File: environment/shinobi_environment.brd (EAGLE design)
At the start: 40.5 x 35 mm, 11 parts

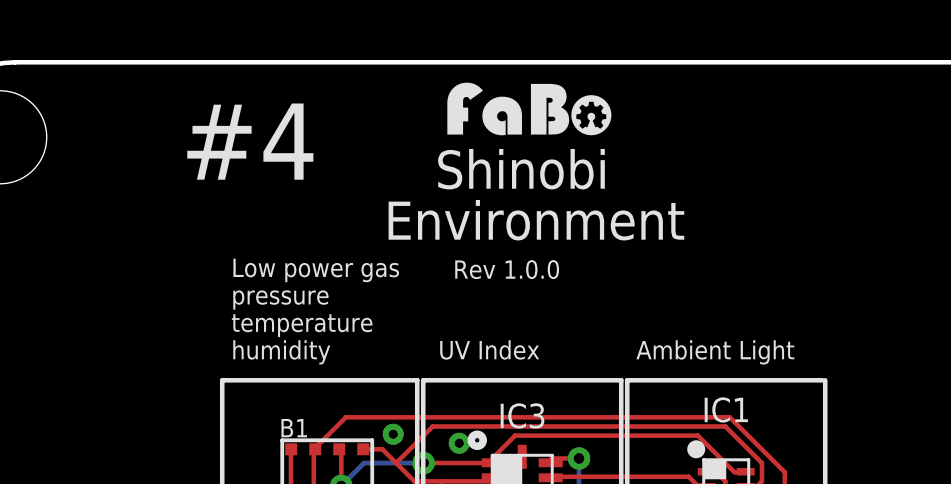
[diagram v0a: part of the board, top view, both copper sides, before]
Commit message: Update BLE with connector.
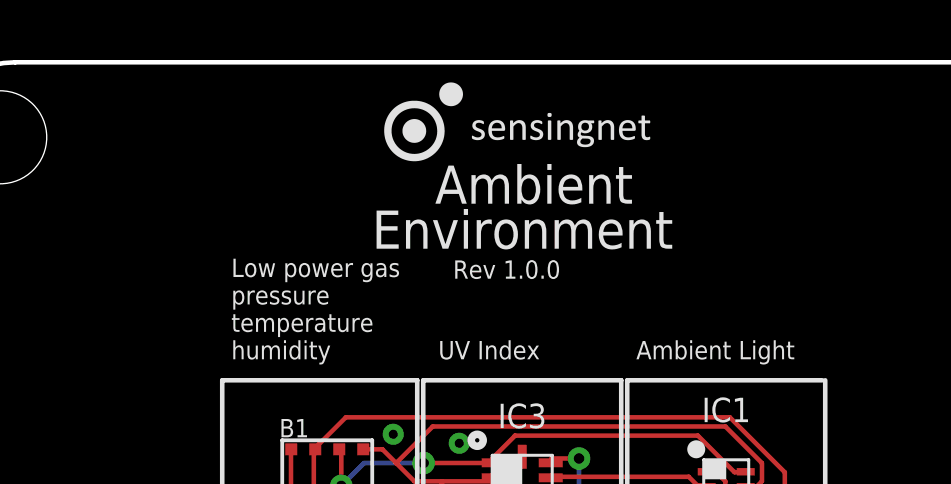
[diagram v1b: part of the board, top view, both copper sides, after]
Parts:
- U$2: device FaBo-Logo:LOGO_FABO_S -> sensingnet:LOGO_WHITE
- moved U$2 4.95 mm to (15.3, 31.7)
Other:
- board text added: "Ambient"
- board text removed: "#4"
- board text removed: "Shinobi"
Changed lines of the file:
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@@
 <?xml version="1.0" encoding="utf-8"?>
 <!DOCTYPE eagle SYSTEM "eagle.dtd">
-<eagle version="8.2.2">
+<eagle version="9.0.0">
 <drawing>
 <settings>
-<setting alwaysvectorfont="no"/>
+<setting alwaysvectorfont="yes"/>
+<setting keepoldvectorfont="yes"/>
 <setting verticaltext="up"/>
 </settings>
@@
 <layers>
 <layer number="1" name="Top" color="4" fill="1" visible="yes" active="yes"/>
+<layer number="2" name="Route2" color="1" fill="3" visible="no" active="yes"/>
+<layer number="15" name="Route15" color="4" fill="6" visible="no" active="yes"/>
 <layer number="16" name="Bottom" color="1" fill="1" visible="yes" active="yes"/>
 <layer number="17" name="Pads" color="2" fill="1" visible="yes" active="yes"/>
@@
 <layer number="59" name="tCarbon" color="7" fill="1" visible="no" active="no"/>
 <layer number="60" name="bCarbon" color="7" fill="1" visible="no" active="no"/>
+<layer number="88" name="SimResults" color="9" fill="1" visible="no" active="no"/>
+<layer number="89" name="SimProbes" color="9" fill="1" visible="no" active="no"/>
 <layer number="90" name="Modules" color="5" fill="1" visible="no" active="no"/>
 <layer number="91" name="Nets" color="2" fill="1" visible="no" active="no"/>
@@
 <board>
 <plain>
-<text x="16.992" y="30.786" size="1.27" layer="21">Shinobi</text>
-<text x="15.292" y="29.086" size="1.27" layer="21">Environment</text>
+<text x="16.992" y="30.286" size="1.27" layer="21">Ambient</text>
+<text x="14.892" y="28.786" size="1.27" layer="21">Environment</text>
 <wire x1="9.9" y1="24.4" x2="16.4" y2="24.4" width="0.1524" layer="21"/>
 <wire x1="16.4" y1="24.4" x2="16.4" y2="14.7" width="0.1524" layer="21"/>
@@
 <wire x1="30" y1="24.4" x2="30" y2="14.7" width="0.1524" layer="21"/>
 <text x="23.7" y="25.1" size="0.6096" layer="21">Ambient Light</text>
-<text x="8.492" y="31.086" size="2.54" layer="21">#4</text>
 <text x="17.592" y="27.786" size="0.6096" layer="21">Rev 1.0.0</text>
 </plain>
@@
 <param name="dpMaxLengthDifference" value="10mm"/>
 <param name="dpGapFactor" value="2.5"/>
-<param name="checkGrid" value="0"/>
 <param name="checkAngle" value="0"/>
 <param name="checkFont" value="1"/>
 <param name="checkRestrict" value="1"/>
+<param name="checkStop" value="0"/>
+<param name="checkValues" value="0"/>
 <param name="useDiameter" value="13"/>
 <param name="maxErrors" value="50"/>
@@
 </autorouter>
 <elements>
-<element name="U$2" library="FaBo-Logo" package="LOGO_FABO_S" value="" x="20.2" y="32.418"/>
 <element name="I2C" library="FaBo-Template" package="FABO_BRICK_I2C_S04B-PASK-2_LONG" value="" x="20.25" y="6.7" rot="R180"/>
 <element name="B1" library="FaBo-Mems" package="BOSCH-BME680" value="" x="13.4" y="20.9"/>
@@
 <element name="C2" library="FaBo-Capacitor" package="0603" value="1uF" x="25.5" y="17"/>
 <element name="U$3" library="FaBo-Template" package="FABO-SHINOBI" value="" x="0" y="0"/>
+<element name="U$2" library="sensingnet" package="LOGO_WHITE" value="" x="15.3" y="31.7"/>
 </elements>
 <signals>

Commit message: シルク削除
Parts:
- removed U$2: (no value), sensingnet:LOGO_WHITE
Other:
- board text removed: "Ambient"
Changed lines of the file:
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@@
 <?xml version="1.0" encoding="utf-8"?>
 <!DOCTYPE eagle SYSTEM "eagle.dtd">
-<eagle version="9.0.0">
+<eagle version="9.6.0">
 <drawing>
 <settings>
-<setting alwaysvectorfont="yes"/>
+<setting alwaysvectorfont="no"/>
 <setting keepoldvectorfont="yes"/>
 <setting verticaltext="up"/>
@@
 <board>
 <plain>
-<text x="16.992" y="30.286" size="1.27" layer="21">Ambient</text>
 <text x="14.892" y="28.786" size="1.27" layer="21">Environment</text>
 <wire x1="9.9" y1="24.4" x2="16.4" y2="24.4" width="0.1524" layer="21"/>
@@
 <param name="checkStop" value="0"/>
 <param name="checkValues" value="0"/>
+<param name="checkNames" value="1"/>
+<param name="checkWireStubs" value="1"/>
+<param name="checkPolygonWidth" value="0"/>
 <param name="useDiameter" value="13"/>
 <param name="maxErrors" value="50"/>
@@
 </autorouter>
 <elements>
-<element name="I2C" library="FaBo-Template" package="FABO_BRICK_I2C_S04B-PASK-2_LONG" value="" x="20.25" y="6.7" rot="R180"/>
-<element name="B1" library="FaBo-Mems" package="BOSCH-BME680" value="" x="13.4" y="20.9"/>
-<element name="C1" library="FaBo-Capacitor" package="0603" value="100nf" x="13.4" y="17.1"/>
-<element name="IC3" library="FaBo-Mems" package="SILICONLABS-SI1133" value="" x="19.9" y="20.9"/>
-<element name="C3" library="FaBo-Capacitor" package="0603" value="0.1uF" x="19" y="17.2" rot="R180"/>
-<element name="R4" library="FaBo-Resistors" package="0603" value="10k" x="21.9" y="18" rot="R90"/>
-<element name="IC1" library="FaBo-Mems" package="INTERSIL-ISL29034" value="" x="26.7" y="21.1"/>
-<element name="R1" library="FaBo-Resistors" package="0603" value="100" x="28.7" y="17.8" rot="R90"/>
-<element name="C2" library="FaBo-Capacitor" package="0603" value="1uF" x="25.5" y="17"/>
-<element name="U$3" library="FaBo-Template" package="FABO-SHINOBI" value="" x="0" y="0"/>
-<element name="U$2" library="sensingnet" package="LOGO_WHITE" value="" x="15.3" y="31.7"/>
+<element name="I2C" library="FaBo-Template" package="FABO_BRICK_I2C_S04B-PASK-2_LONG" value="" x="20.25" y="6.7" smashed="yes" rot="R180">
+<attribute name="NAME" x="20.25" y="10.51" size="0.8128" layer="25" font="vector" ratio="12" align="bottom-center"/>
+</element>
+<element name="B1" library="FaBo-Mems" package="BOSCH-BME680" value="" x="13.4" y="20.9" smashed="yes">
+<attribute name="NAME" x="11.8" y="22.5" size="0.6096" layer="25"/>
+</element>
+<element name="C1" library="FaBo-Capacitor" package="0603" value="100nf" x="13.4" y="17.1" smashed="yes">
+<attribute name="NAME" x="13.4" y="17.989" size="0.8128" layer="25" font="vector" ratio="12" align="bottom-center"/>
+<attribute name="VALUE" x="13.4" y="17.1" size="0.8128" layer="27" font="vector" ratio="12" align="center"/>
+</element>
+<element name="IC3" library="FaBo-Mems" package="SILICONLABS-SI1133" value="" x="19.9" y="20.9" smashed="yes">
+<attribute name="NAME" x="19.9" y="22.805" size="0.8128" layer="21" font="vector" ratio="12" align="bottom-center"/>
+</element>
+<element name="C3" library="FaBo-Capacitor" package="0603" value="0.1uF" x="19" y="17.2" smashed="yes" rot="R180">
+<attribute name="NAME" x="19" y="16.311" size="0.8128" layer="25" font="vector" ratio="12" rot="R180" align="bottom-center"/>
+<attribute name="VALUE" x="19" y="17.2" size="0.8128" layer="27" font="vector" ratio="12" rot="R180" align="center"/>
+</element>
+<element name="R4" library="FaBo-Resistors" package="0603" value="10k" x="21.9" y="18" smashed="yes" rot="R90">
+<attribute name="NAME" x="21.011" y="18" size="0.8128" layer="25" font="vector" ratio="12" rot="R90" align="bottom-center"/>
+<attribute name="VALUE" x="21.9" y="18" size="0.8128" layer="27" font="vector" ratio="12" rot="R90" align="center"/>
+</element>
+<element name="IC1" library="FaBo-Mems" package="INTERSIL-ISL29034" value="" x="26.7" y="21.1" smashed="yes">
+<attribute name="NAME" x="26.7" y="23.005" size="0.8128" layer="25" font="vector" ratio="12" rot="SR0" align="bottom-center"/>
+</element>
+<element name="R1" library="FaBo-Resistors" package="0603" value="100" x="28.7" y="17.8" smashed="yes" rot="R90">
+<attribute name="NAME" x="27.811" y="17.8" size="0.8128" layer="25" font="vector" ratio="12" rot="R90" align="bottom-center"/>
+<attribute name="VALUE" x="28.7" y="17.8" size="0.8128" layer="27" font="vector" ratio="12" rot="R90" align="center"/>
+</element>
+<element name="C2" library="FaBo-Capacitor" package="0603" value="1uF" x="25.5" y="17" smashed="yes">
+<attribute name="NAME" x="25.5" y="17.889" size="0.8128" layer="25" font="vector" ratio="12" align="bottom-center"/>
+<attribute name="VALUE" x="25.5" y="17" size="0.8128" layer="27" font="vector" ratio="12" align="center"/>
+</element>
+<element name="U$3" library="FaBo-Template" package="FABO-SHINOBI" value="" x="0" y="0" smashed="yes"/>
 </elements>
 <signals>
@@
 </signal>
 </signals>
+<mfgpreviewcolors>
+<mfgpreviewcolor name="soldermaskcolor" color="0xC8008000"/>
+<mfgpreviewcolor name="silkscreencolor" color="0xFFFEFEFE"/>
+<mfgpreviewcolor name="backgroundcolor" color="0xFF282828"/>
+<mfgpreviewcolor name="coppercolor" color="0xFFFFBF00"/>
+<mfgpreviewcolor name="substratecolor" color="0xFF786E46"/>
+</mfgpreviewcolors>
 </board>
 </drawing>

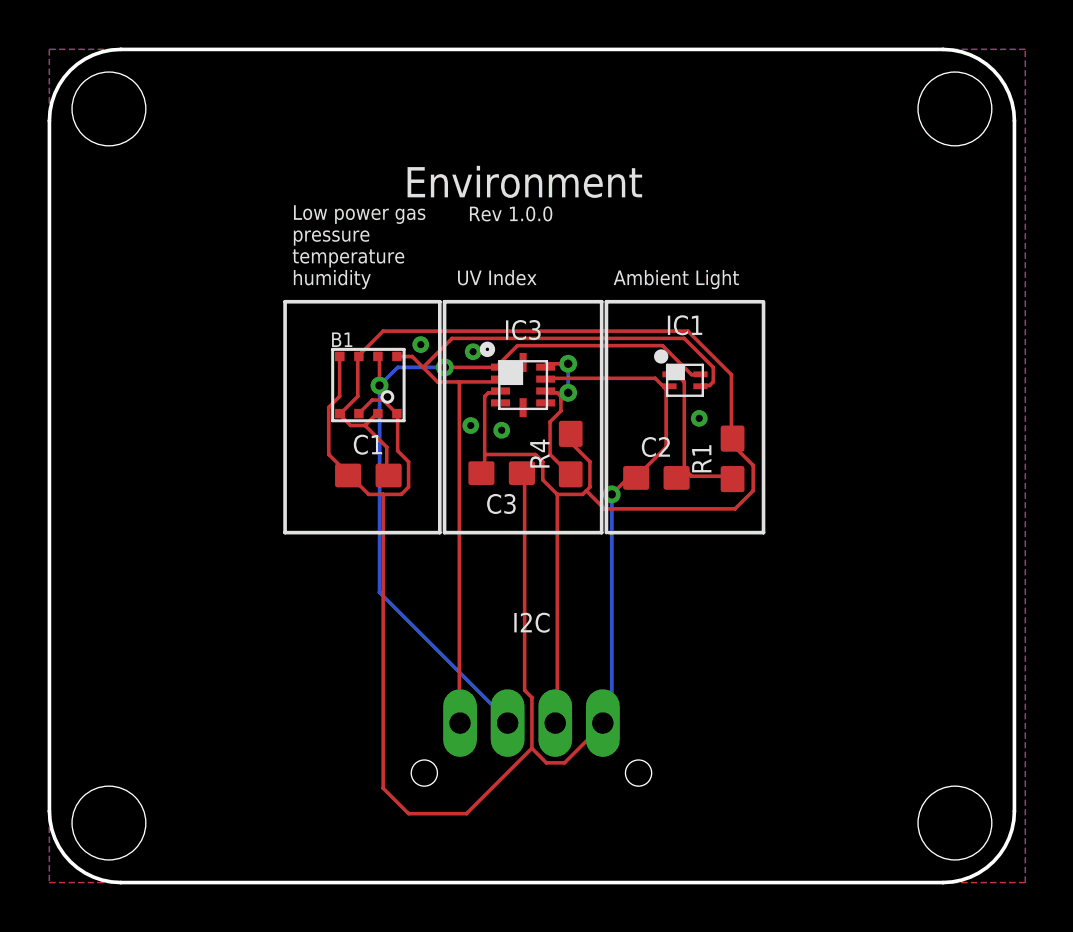
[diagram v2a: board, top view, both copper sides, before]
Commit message: #21 Shinobi Enviroment 1.0.1 アップデート　VCC ５V対応　LDO、レベル変換、BME６８０通風口追加、番号の変更　４から２１
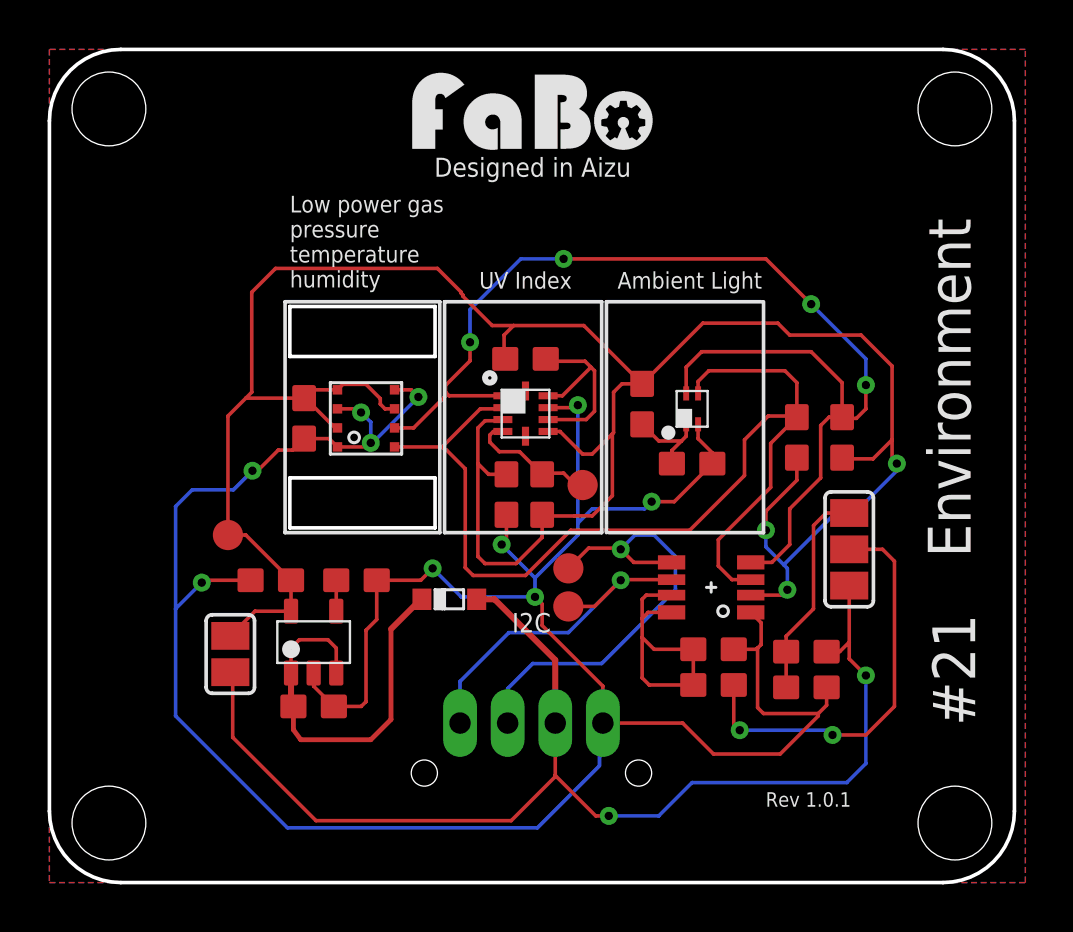
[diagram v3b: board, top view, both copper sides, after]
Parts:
- added C4: 0.01uF, FaBo-Capacitor:0603
- added C5: 1uF, FaBo-Capacitor:0603
- added C6: 4.7uF, FaBo-Capacitor:0603
- added C7: 0.1uF, FaBo-Capacitor:0603
- added IC2: (no value), FaBo-Supply:SOT-23-5
- added R2: 10k, FaBo-Resistors:0603
- added R3: 200k, FaBo-Resistors:0603
- added R5, R6: 4.7k, FaBo-Resistors:0603
- added R7: 1.8k, FaBo-Resistors:0603
- added R8: 3.3k, FaBo-Resistors:0603
- added SJ1: (no value), jumper:SJ_2
- added SJ2: (no value), jumper:SJ
- added TP1, TP2, TP3, TP4: TPB1,27, testpad:B1,27
- added U$14: (no value), FaBo-etc:LOGO_FABO_MS
- added U$2: CUS05F40, FaBo-Diode:CUS05F40
- added U4: PCA9306DP1, FaBo-LevelTranslator:TSSOP8
- moved R1 4.44 mm to (24.9, 20.1)
- moved R4 4.43 mm to (20.0, 22.0), turned to 180 degrees
- moved C1 3.61 mm to (10.7, 19.5), turned to 90 degrees
- moved C2 1.62 mm to (27.0, 17.6), turned to 180 degrees
- moved B1 1.40 mm to (13.3, 19.5), turned to 270 degrees
- moved IC1 1.24 mm to (27.0, 19.9), turned to 90 degrees
- moved IC3 1.20 mm to (20.0, 19.7)
- moved C3 0.92 mm to (19.2, 16.3), turned to 90 degrees
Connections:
- new net 3.3V: R7.1, R8.2, SJ1.3
- new net 5V: I2C.VCC, R7.2, SJ1.1, SJ2.1, U$2.A
- new net N$2: C4.2, IC2.4
- new net N$3: C5.2, IC2.1, IC2.3, U$2.C
- new net N$5: IC3.4, R2.1, TP4.TP
- new net N$8: C7.2, R3.1, U4.EN, U4.VREF2
- new net N$9: R3.2, SJ1.2
- new net SCL_HV: I2C.SCL, TP1.TP, U4.SCL2
- new net SDA_HV: I2C.SDA, TP2.TP, U4.SDA2
- net +3V3: now also C6.2, IC2.5, IC3.6, R2.2, R5.2, R6.2, SJ2.2, TP3.TP, U4.VREF1; no longer I2C.VCC
- net GND: now also C4.1, C5.1, C6.1, C7.1, IC2.2, R8.1, U4.GND
- net SCL: now also R5.1, U4.SCL1; no longer I2C.SCL
- net SDA: now also R6.1, U4.SDA1; no longer I2C.SDA
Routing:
- net 5V: track 0.00 -> 51.3 mm, vias 0 -> 2
- net +3V3: track 59.2 -> 106.2 mm, vias 0 -> 3
- net GND: track 70.5 -> 115.0 mm, vias 6 -> 10
- net SDA_HV: track 0.00 -> 19.5 mm, vias 0 -> 1
- net SDA: track 32.7 -> 50.2 mm, vias 2 -> 4
- net N$9: track 0.00 -> 17.3 mm, vias 0 -> 2
- net N$3: track 0.00 -> 17.2 mm
- net SCL_HV: track 0.00 -> 15.1 mm, vias 0 -> 1
- net N$8: track 0.00 -> 12.1 mm
- net SCL: track 33.6 -> 44.2 mm
- net 3.3V: track 0.00 -> 8.99 mm
- net N$5: track 0.00 -> 5.60 mm
- net VCC: track 7.56 -> 3.91 mm
- net N$2: track 0.00 -> 1.30 mm
- net N$4: track 7.30 -> 8.35 mm, vias 2 -> 0
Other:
- board text added: "#21"
- board text added: "Designed in Aizu"
- board text added: "Rev 1.0.1"
- board text removed: "Rev 1.0.0"

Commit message: ファイル削除
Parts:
- removed R4: 10k, FaBo-Resistors:0603
- removed R7: 1.8k, FaBo-Resistors:0603
- removed R8: 3.3k, FaBo-Resistors:0603
- added C8: 100nf, FaBo-Capacitor:0603
- moved U$2 10.0 mm to (12.6, 2.80)
- moved IC2 3.20 mm to (11.2, 6.90)
- moved C5 3.20 mm to (11.1, 4.20)
- moved C4 3.14 mm to (12.4, 9.60)
- moved C6 3.10 mm to (9.20, 9.60)
- moved SJ2 3.04 mm to (8.10, 6.60)
- moved IC1 0.20 mm to (26.8, 19.9)
- renumbered TP4 to INT
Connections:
- removed net 3.3V: R7.1, R8.2, SJ1.3
- removed net N$4: IC3.7, IC3.9, R4.1
- net +3V3: now also C8.2, IC3.7, IC3.9, SJ1.3; no longer R4.2
- net 5V: no longer R7.2
- net GND: now also C8.1; no longer R8.1
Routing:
- net GND: track 115.0 -> 288.2 mm, vias 10 -> 74
- net +3V3: track 106.2 -> 128.5 mm
- net N$3: track 17.2 -> 8.17 mm
- net 3.3V: track 8.99 -> 0.00 mm
- net N$4: track 8.35 -> 0.00 mm
- net 5V: track 51.3 -> 47.3 mm
- net SDA: track 50.2 -> 51.1 mm
- net SCL_HV: track 15.1 -> 15.8 mm
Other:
- board text added: "1"
- board text added: "3"
- board text added: "Low power gas Air pressure Temperature Humidity"
- board text added: "VREF2"
- board text removed: "Low power gas pressure temperature humidity"
